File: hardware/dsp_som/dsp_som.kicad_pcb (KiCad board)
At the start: 6 copper layers, 40 x 60 mm, 60 parts, among them J1 Micro_SD_Card_Det_Hirose_DM3AT, J2 SWD, J3 Conn_02x22_Odd_Even, U1 IS42S16400J-xT, U2 SGTL5000XNAA3, U4 BU18SD2MG-MTR, U5 STM32F446ZCTx, Y1 16MHz, Y3 32kHz768

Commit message: silkscreen again
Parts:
- added ?: , clipboard:abc97075-b19d-4899-8b32-22833b0b5e2d, F.Cu at (123.3, 58.6)

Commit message: gnd vias
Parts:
- J3: value Conn_02x22_Odd_Even -> DSP_SoM Connector
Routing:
- net /DQ14: track 25.3 -> 26.9 mm
- net /DQ1: track 18.8 -> 19.6 mm
- net /CODEC_DOUT: track 38.8 -> 39.5 mm
- net /DQ0: track 16.7 -> 17.2 mm
- net GND: vias 54 -> 187

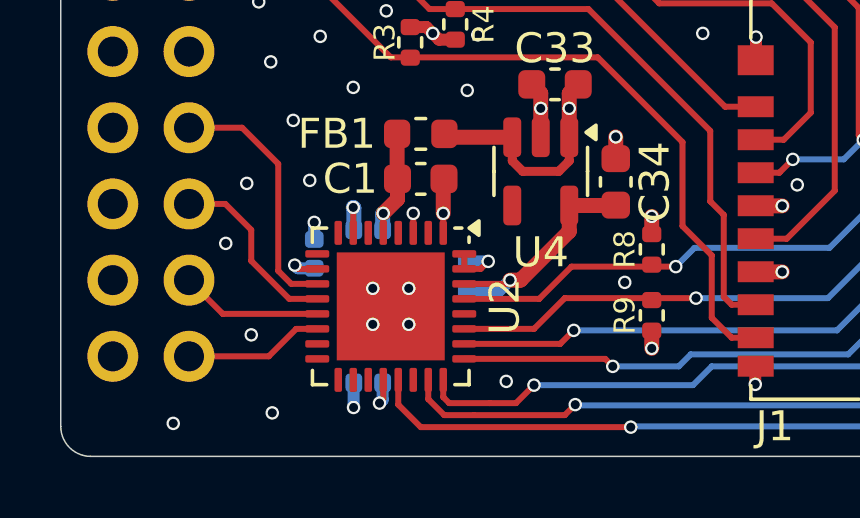
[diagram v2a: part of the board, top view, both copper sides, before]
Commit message: Change SGTL5000 model due to obsolescence
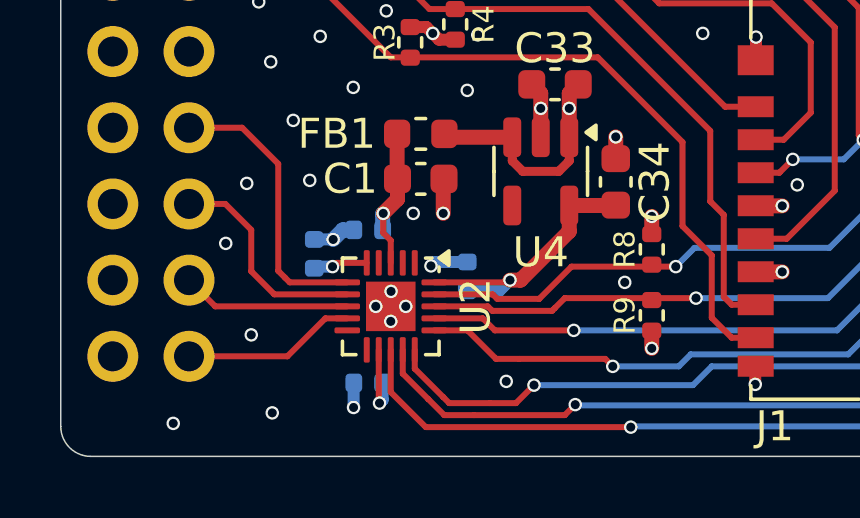
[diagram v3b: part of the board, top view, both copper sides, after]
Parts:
- U2: value SGTL5000XNAA3 -> SGTL5000XNLA3; footprint Package_DFN_QFN:QFN-32-1EP_5x5mm_P0.5mm_EP3.6x3.6mm -> Package_DFN_QFN:QFN-20-1EP_3x3mm_P0.4mm_EP1.65x1.65mm
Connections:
- U2 pad 1: GND -> unconnected-(U2-HP_R-Pad1)
- U2 pad 10: /VAG -> unconnected-(U2-MIC-Pad10)
- U2 pad 11: /LINEOUT_R -> unconnected-(U2-MIC_BIAS-Pad11)
- U2 pad 12: /LINEOUT_L -> +3.3V
- U2 pad 13: /LINEIN_R -> /CODEC_MCLK
- U2 pad 14: /LINEIN_L -> /CODEC_LRCLK
- U2 pad 15: unconnected-(U2-MIC-Pad15) -> /CODEC_SCLK
- U2 pad 16: unconnected-(U2-MIC_BIAS-Pad16) -> /CODEC_DOUT
- U2 pad 17: unconnected-(U2-NC-Pad17) -> /CODEC_DIN
- U2 pad 18: unconnected-(U2-CPFILT-Pad18) -> /CODEC_SDA
- U2 pad 19: unconnected-(U2-NC-Pad19) -> /CODEC_SCL
- U2 pad 20: +3.3V -> +1V8
- U2 pad 21: /CODEC_MCLK -> GND
- U2 pad 3: GND -> +3.3VA
- U2 pad 5: +3.3VA -> /VAG
- U2 pad 6: unconnected-(U2-HP_L-Pad6) -> /LINEOUT_R
- U2 pad 7: GND -> /LINEOUT_L
- U2 pad 8: unconnected-(U2-NC-Pad8) -> /LINEIN_R
- U2 pad 9: unconnected-(U2-NC-Pad9) -> /LINEIN_L
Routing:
- net GND: track 68.0 -> 65.2 mm, vias 187 -> 186
- net /CODEC_SCLK: track 45.0 -> 46.3 mm
- net /CODEC_DOUT: track 39.5 -> 40.9 mm
- net /CODEC_LRCLK: track 46.8 -> 48.2 mm
- net /LINEIN_L: track 4.65 -> 5.80 mm
- net /LINEOUT_L: track 6.19 -> 7.33 mm
- net +3.3VA: track 46.7 -> 47.8 mm
- net /CODEC_SCL: track 33.5 -> 34.5 mm
- net /CODEC_MCLK: track 49.0 -> 50.0 mm
- net /LINEOUT_R: track 8.52 -> 9.50 mm
- net +1V8: track 8.21 -> 9.19 mm
- net /CODEC_DIN: track 39.4 -> 40.4 mm
- net +3.3V: track 61.6 -> 62.5 mm
- net /LINEIN_R: track 4.74 -> 5.64 mm
- net /CODEC_SDA: track 35.7 -> 36.5 mm
